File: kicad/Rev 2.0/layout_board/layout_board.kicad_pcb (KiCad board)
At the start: 2 copper layers, 309.6 x 95.2 mm, 216 parts, among them U0:0 GH39FKSW, U0:1 GH39FKSW, U0:10 GH39FKSW, U0:11 GH39FKSW, U0:12 GH39FKSW, U0:13 GH39FKSW, U0:14 GH39FKSW, U0:2 GH39FKSW, U0:3 GH39FKSW, U0:4 GH39FKSW, U0:5 GH39FKSW, U0:6 GH39FKSW, U0:7 GH39FKSW, U0:8 GH39FKSW, U0:9 GH39FKSW, U1 CD4067BPWR, U1:0 GH39FKSW, U1:1 GH39FKSW, U1:10 GH39FKSW, U1:11 GH39FKSW, U1:12 GH39FKSW, U1:13 GH39FKSW, U1:14 GH39FKSW, U1:2 GH39FKSW, U1:3 GH39FKSW, U1:4 GH39FKSW, U1:5 GH39FKSW, U1:6 GH39FKSW, U1:7 GH39FKSW, U1:8 GH39FKSW, U1:9 GH39FKSW, U2 CD4067BPWR, U2:0 GH39FKSW, U2:1 GH39FKSW, U2:10 GH39FKSW, U2:11 GH39FKSW, U2:12 GH39FKSW, U2:13 GH39FKSW, U2:2 GH39FKSW, U2:3 GH39FKSW, U2:4 GH39FKSW, U2:5 GH39FKSW, U2:6 GH39FKSW, U2:7 GH39FKSW, U2:8 GH39FKSW, U2:9 GH39FKSW, U3 CD4067BPWR, U3:1 GH39FKSW, U3:10 GH39FKSW, U3:11 GH39FKSW, U3:12 GH39FKSW, U3:13 GH39FKSW, U3:2 GH39FKSW, U3:3 GH39FKSW, U3:4 GH39FKSW, U3:5 GH39FKSW, U3:6 GH39FKSW, U3:7 GH39FKSW, U3:8 GH39FKSW, U3:9 GH39FKSW, U4 CD4067BPWR, U4:1 GH39FKSW, U4:10 GH39FKSW, U4:12 GH39FKSW, U4:13 GH39FKSW, U4:14 GH39FKSW, U4:2 GH39FKSW, U4:3 GH39FKSW, U4:5 GH39FKSW, U4:7 GH39FKSW, U4:9 GH39FKSW, U5 CD4067BPWR

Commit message: wip: rev 2.0 pcb
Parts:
- removed C1, C10, C11, C12, C13, C14, C15, C16, C17, C18, C19, C2, C20, C21, C22, C23, C24, C25, C26, C27, C28, C29, C3, C30, C31, C32, C33, C34, C35, C36, C37, C38, C39, C4, C40, C41, C42, C43, C44, C45, C46, C47, C48, C49, C5, C50, C51, C52, C53, C54, C55, C56, C57, C58, C59, C6, C60, C61, C62, C63, C64, C65, C66, C67, C7, C8, C9: 100n, Capacitor_SMD:C_0402_1005Metric_Pad0.74x0.62mm_HandSolder
- moved U3 22.0 mm to (187.2, 66.7)
- moved U5 20.6 mm to (308.0, 66.7)
- moved U4 20.6 mm to (241.3, 66.7)
- moved C69 20.5 mm to (126.6, 62.2), turned to 180 degrees
- moved U2 19.6 mm to (133.3, 66.7)
- moved U1 16.1 mm to (69.3, 66.7)
- moved C68 14.1 mm to (64.7, 61.9), turned to 180 degrees
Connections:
- U0:0 pad 2: unconnected-(U0:0-VOUT-Pad2) -> /AMUX0:10
- U0:1 pad 2: unconnected-(U0:1-VOUT-Pad2) -> /AMUX0:9
- U0:2 pad 2: unconnected-(U0:2-VOUT-Pad2) -> /AMUX0:7
- U0:3 pad 2: unconnected-(U0:3-VOUT-Pad2) -> /AMUX0:6
- U1 pad 16: /AMUX0:15 -> unconnected-(U1-15-Pad16)
- U1 pad 17: /AMUX0:14 -> unconnected-(U1-14-Pad17)
- U1:0 pad 2: unconnected-(U1:0-VOUT-Pad2) -> /AMUX0:11
- U1:1 pad 2: unconnected-(U1:1-VOUT-Pad2) -> /AMUX0:8
- U1:2 pad 2: unconnected-(U1:2-VOUT-Pad2) -> /AMUX0:5
- U2 pad 16: /AMUX1:15 -> unconnected-(U2-15-Pad16)
- U2 pad 17: /AMUX1:14 -> unconnected-(U2-14-Pad17)
- U2 pad 18: /AMUX1:13 -> unconnected-(U2-13-Pad18)
- U2:0 pad 2: unconnected-(U2:0-VOUT-Pad2) -> /AMUX0:12
- U2:1 pad 2: unconnected-(U2:1-VOUT-Pad2) -> /AMUX0:1
- U2:2 pad 2: unconnected-(U2:2-VOUT-Pad2) -> /AMUX0:4
- U3 pad 16: /AMUX2:15 -> unconnected-(U3-15-Pad16)
- U3 pad 17: /AMUX2:14 -> unconnected-(U3-14-Pad17)
- U3 pad 18: /AMUX2:13 -> unconnected-(U3-13-Pad18)
- U3:1 pad 2: unconnected-(U3:1-VOUT-Pad2) -> /AMUX0:0
- U3:2 pad 2: unconnected-(U3:2-VOUT-Pad2) -> /AMUX0:2
- U4 pad 16: /AMUX3:15 -> unconnected-(U4-15-Pad16)
- U4 pad 17: /AMUX3:14 -> unconnected-(U4-14-Pad17)
- U4 pad 18: /AMUX3:13 -> unconnected-(U4-13-Pad18)
- U4:1 pad 2: unconnected-(U4:1-VOUT-Pad2) -> /AMUX0:13
- U4:2 pad 2: unconnected-(U4:2-VOUT-Pad2) -> /AMUX0:3
- U5 pad 16: /AMUX4:15 -> unconnected-(U5-15-Pad16)
- U5 pad 17: /AMUX4:14 -> unconnected-(U5-14-Pad17)
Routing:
- net /AMUX0:3: track 0.00 -> 59.1 mm
- net /AMUX0:13: track 0.00 -> 52.4 mm
- net /AMUX0:6: track 0.00 -> 41.1 mm
- net /AMUX0:10: track 0.00 -> 40.6 mm
- net /AMUX0:2: track 0.00 -> 33.8 mm
- net /AMUX0:7: track 0.00 -> 33.5 mm
- net /AMUX0:0: track 0.00 -> 33.5 mm
- net /AMUX0:11: track 0.00 -> 32.5 mm
- net /AMUX0:12: track 0.00 -> 31.9 mm
- net /AMUX0:9: track 0.00 -> 31.7 mm
- net /SELECT2: track 219.5 -> 248.0 mm, vias 0 -> 5
- net /AMUX0:4: track 0.00 -> 27.0 mm
- net /SELECT1: track 219.1 -> 245.6 mm, vias 0 -> 5
- net /SELECT3: track 220.7 -> 245.3 mm, vias 0 -> 5
- net /AMUX0:5: track 0.00 -> 22.3 mm
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- added copper zone on F.Cu, net GND

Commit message: wip: rev 2.0 pcb
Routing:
- net +3.3VA: track 5.45 -> 246.7 mm
- net /AMUX0:5: track 22.3 -> 23.1 mm
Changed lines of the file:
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@@
 		(fp_arc
 			(start 9.03125 8.000001)
-			(mid 8.677693 7.853543)
+			(mid 8.677729 7.853537)
 			(end 8.53125 7.500001)
 			(stroke
@@
 		(fp_arc
 			(start 14.780039 -5.999999)
-			(mid 15.133602 -5.853545)
+			(mid 15.133567 -5.853539)
 			(end 15.280039 -5.499999)
 			(stroke
@@
 		(fp_arc
 			(start 15.28125 7.500001)
-			(mid 15.1348 7.853536)
+			(mid 15.134806 7.853571)
 			(end 14.78125 8.000001)
 			(stroke
@@
 		(fp_arc
 			(start 15.28125 7.500001)
-			(mid 15.1348 7.853536)
+			(mid 15.134806 7.853571)
 			(end 14.78125 8.000001)
 			(stroke
@@
 		(fp_arc
 			(start 14.780039 -5.999999)
-			(mid 15.133602 -5.853545)
+			(mid 15.133567 -5.853539)
 			(end 15.280039 -5.499999)
 			(stroke
@@
 		(fp_arc
 			(start 9.03125 8.000001)
-			(mid 8.677693 7.853543)
+			(mid 8.677729 7.853537)
 			(end 8.53125 7.500001)
 			(stroke
@@
 		(fp_arc
 			(start 15.28125 7.500001)
-			(mid 15.1348 7.853536)
+			(mid 15.134806 7.853571)
 			(end 14.78125 8.000001)
 			(stroke
@@
 		(fp_arc
 			(start 14.780039 -5.999999)
-			(mid 15.133602 -5.853545)
+			(mid 15.133567 -5.853539)
 			(end 15.280039 -5.499999)
 			(stroke
@@
 		(fp_arc
 			(start 9.03125 8.000001)
-			(mid 8.677693 7.853543)
+			(mid 8.677729 7.853537)
 			(end 8.53125 7.500001)
 			(stroke
@@
 		(fp_arc
 			(start 9.03125 8.000001)
-			(mid 8.677693 7.853543)
+			(mid 8.677729 7.853537)
 			(end 8.53125 7.500001)
 			(stroke
@@
 		(fp_arc
 			(start 14.780039 -5.999999)
-			(mid 15.133602 -5.853545)
+			(mid 15.133567 -5.853539)
 			(end 15.280039 -5.499999)
 			(stroke
@@
 		(fp_arc
 			(start 15.28125 7.500001)
-			(mid 15.1348 7.853536)
+			(mid 15.134806 7.853571)
 			(end 14.78125 8.000001)
 			(stroke
@@
 		(tags "capacitor handsolder")
 		(property "Reference" "C68"
-			(at 0 1.16 360)
+			(at 0 1.16 0)
 			(layer "B.SilkS")
 			(effects
@@
 		)
 		(property "Value" "100n"
-			(at 0 -1.16 360)
+			(at 0 -1.16 0)
 			(layer "B.Fab")
 			(effects
@@
 		)
 		(fp_text user "${REFERENCE}"
-			(at 0 0 360)
+			(at 0 0 0)
 			(layer "B.Fab")
 			(effects
@@
 		(tags "capacitor handsolder")
 		(property "Reference" "C69"
-			(at 0 1.16 360)
+			(at 0 1.16 0)
 			(layer "B.SilkS")
 			(effects
@@
 		)
 		(property "Value" "100n"
-			(at 0 -1.16 360)
+			(at 0 -1.16 0)
 			(layer "B.Fab")
 			(effects
@@
 		)
 		(fp_text user "${REFERENCE}"
-			(at 0 0 360)
+			(at 0 0 0)
 			(layer "B.Fab")
 			(effects
@@
 	)
 	(segment
+		(start 127.208669 71.402118)
+		(end 131.971169 76.164618)
+		(width 0.5)
+		(layer "B.Cu")
+		(net 2)
+	)
+	(segment
+		(start 153.402419 107.120868)
+		(end 153.402419 114.264618)
+		(width 0.5)
+		(layer "B.Cu")
+		(net 2)
+	)
+	(segment
+		(start 155.974294 38.064618)
+		(end 165.308669 47.398993)
+		(width 0.5)
+		(layer "B.Cu")
+		(net 2)
+	)
+	(segment
+		(start 151.021169 76.164618)
+		(end 141.496169 85.689618)
+		(width 0.5)
+		(layer "B.Cu")
+		(net 2)
+	)
+	(segment
+		(start 167.877984 73.971433)
+		(end 170.071169 76.164618)
+		(width 0.5)
+		(layer "B.Cu")
+		(net 2)
+	)
+	(segment
+		(start 117.683669 38.064618)
+		(end 127.208669 47.589618)
+		(width 0.5)
+		(layer "B.Cu")
+		(net 2)
+	)
+	(segment
+		(start 160.546169 85.689618)
+		(end 160.546169 95.214618)
+		(width 0.5)
+		(layer "B.Cu")
+		(net 2)
+	)
+	(segment
+		(start 146.258669 57.114618)
+		(end 146.258669 71.402118)
+		(width 0.5)
+		(layer "B.Cu")
+		(net 2)
+	)
+	(segment
 		(start 66.457912 63.099887)
 		(end 65.30768 61.949655)
@@
 	)
 	(segment
-		(start 130.569852 63.099887)
-		(end 128.072704 63.099887)
+		(start 146.258669 47.589618)
+		(end 146.258669 57.114618)
 		(width 0.5)
 		(layer "B.Cu")
@@
 	)
 	(segment
-		(start 128.072704 63.099887)
-		(end 127.182921 62.210104)
+		(start 167.877984 59.683933)
+		(end 167.877984 73.971433)
+		(width 0.5)
+		(layer "B.Cu")
+		(net 2)
+	)
+	(segment
+		(start 127.208669 57.114618)
+		(end 127.208669 71.402118)
+		(width 0.5)
+		(layer "B.Cu")
+		(net 2)
+	)
+	(segment
+		(start 122.446169 95.214618)
+		(end 120.064919 97.595868)
+		(width 0.5)
+		(layer "B.Cu")
+		(net 2)
+	)
+	(segment
+		(start 120.064919 97.595868)
+		(end 120.064919 114.264618)
+		(width 0.5)
+		(layer "B.Cu")
+		(net 2)
+	)
+	(segment
+		(start 165.308669 57.114618)
+		(end 167.877984 59.683933)
 		(width 0.5)
 		(layer "B.Cu")
@@
 	)
 	(segment
+		(start 165.308669 47.398993)
+		(end 165.308669 57.114618)
+		(width 0.5)
+		(layer "B.Cu")
+		(net 2)
+	)
+	(segment
+		(start 122.446169 85.689618)
+		(end 122.446169 95.214618)
+		(width 0.5)
+		(layer "B.Cu")
+		(net 2)
+	)
+	(segment
+		(start 136.733669 38.064618)
+		(end 146.258669 47.589618)
+		(width 0.5)
+		(layer "B.Cu")
+		(net 2)
+	)
+	(segment
+		(start 131.971169 76.164618)
+		(end 122.446169 85.689618)
+		(width 0.5)
+		(layer "B.Cu")
+		(net 2)
+	)
+	(segment
+		(start 141.496169 95.214618)
+		(end 153.402419 107.120868)
+		(width 0.5)
+		(layer "B.Cu")
+		(net 2)
+	)
+	(segment
 		(start 66.47268 63.099887)
 		(end 66.457912 63.099887)
@@
 	)
 	(segment
+		(start 127.208669 47.589618)
+		(end 127.208669 57.114618)
+		(width 0.5)
+		(layer "B.Cu")
+		(net 2)
+	)
+	(segment
+		(start 141.496169 85.689618)
+		(end 141.496169 95.214618)
+		(width 0.5)
+		(layer "B.Cu")
+		(net 2)
+	)
+	(segment
+		(start 170.071169 76.164618)
+		(end 160.546169 85.689618)
+		(width 0.5)
+		(layer "B.Cu")
+		(net 2)
+	)
+	(segment
+		(start 146.258669 71.402118)
+		(end 151.021169 76.164618)
+		(width 0.5)
+		(layer "B.Cu")
+		(net 2)
+	)
+	(segment
 		(start 65.296169 61.938144)
 		(end 65.30768 61.949655)
@@
 	)
 	(segment
-		(start 79.722588 65.049849)
-		(end 89.001268 55.771169)
+		(start 90.452118 57.185258)
+		(end 90.452118 55.771169)
 		(width 0.3)
 		(layer "B.Cu")
@@
 	)
 	(segment
-		(start 72.032752 65.049849)
-		(end 79.722588 65.049849)
+		(start 82.587527 65.049849)
+		(end 90.452118 57.185258)
 		(width 0.3)
 		(layer "B.Cu")
@@
 	)
 	(segment
-		(start 89.001268 55.771169)
-		(end 90.452118 55.771169)
+		(start 72.032752 65.049849)
+		(end 82.587527 65.049849)
 		(width 0.3)
 		(layer "B.Cu")
@@
 	)
 	(segment
-		(start 39.84654 38.503091)
-		(end 38.064618 36.721169)
+		(start 66.47268 65.049849)
+		(end 65.049849 65.049849)
 		(width 0.3)
 		(layer "B.Cu")
@@
 	)
 	(segment
-		(start 65.681684 65.049849)
-		(end 39.84654 39.214705)
+		(start 65.049849 65.049849)
+		(end 39.84654 39.84654)
 		(width 0.3)
 		(layer "B.Cu")
@@
 	)
 	(segment
-		(start 66.47268 65.049849)
-		(end 65.681684 65.049849)
+		(start 39.84654 38.503091)
+		(end 38.064618 36.721169)
 		(width 0.3)
 		(layer "B.Cu")
@@
 	)
 	(segment
-		(start 39.84654 39.214705)
+		(start 39.84654 39.84654)
 		(end 39.84654 38.503091)
 		(width 0.3)

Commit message: wip: rev 2.0 pcb
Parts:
- moved U5 24.4 mm to (300.0, 43.6), turned to 90 degrees
- moved U2 23.5 mm to (128.9, 43.6), turned to 90 degrees
- moved U1 23.1 mm to (71.5, 43.6), turned to 90 degrees
- moved U4 23.1 mm to (242.9, 43.6), turned to 90 degrees
- moved U3 23.1 mm to (185.7, 43.6), turned to 90 degrees
- moved C71 18.3 mm to (245.0, 49.5)
- moved C70 18.1 mm to (187.9, 49.5)
- moved C68 15.3 mm to (73.7, 49.6)
- moved C69 13.4 mm to (131.2, 49.6)
- moved C72 9.25 mm to (302.2, 49.6), turned to 180 degrees
- turned U0:11 to -45 degrees
- turned U0:14 to -45 degrees
- turned U0:2 to -45 degrees
- turned U0:3 to -45 degrees
- turned U0:5 to -45 degrees
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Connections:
- U0:0 pad 2: /AMUX0:10 -> /AMUX0:1
- U0:1 pad 2: /AMUX0:9 -> /AMUX0:0
- U0:10 pad 2: unconnected-(U0:10-VOUT-Pad2) -> /AMUX3:0
- U0:11 pad 2: unconnected-(U0:11-VOUT-Pad2) -> /AMUX3:12
- U0:12 pad 2: unconnected-(U0:12-VOUT-Pad2) -> /AMUX4:1
- U0:13 pad 2: unconnected-(U0:13-VOUT-Pad2) -> /AMUX4:0
- U0:14 pad 2: unconnected-(U0:14-VOUT-Pad2) -> /AMUX4:13
- U0:2 pad 2: /AMUX0:7 -> /AMUX0:13
- U0:3 pad 2: /AMUX0:6 -> /AMUX0:12
- U0:4 pad 2: unconnected-(U0:4-VOUT-Pad2) -> /AMUX1:0
- U0:5 pad 2: unconnected-(U0:5-VOUT-Pad2) -> /AMUX1:12
- U0:6 pad 2: unconnected-(U0:6-VOUT-Pad2) -> /AMUX2:1
- U0:7 pad 2: unconnected-(U0:7-VOUT-Pad2) -> /AMUX2:0
- U0:8 pad 2: unconnected-(U0:8-VOUT-Pad2) -> /AMUX2:12
- U0:9 pad 2: unconnected-(U0:9-VOUT-Pad2) -> /AMUX3:1
- U1:0 pad 2: /AMUX0:11 -> /AMUX0:2
- U1:1 pad 2: /AMUX0:8 -> /AMUX0:7
- U1:10 pad 2: unconnected-(U1:10-VOUT-Pad2) -> /AMUX3:7
- U1:11 pad 2: unconnected-(U1:11-VOUT-Pad2) -> /AMUX3:11
- U1:12 pad 2: unconnected-(U1:12-VOUT-Pad2) -> /AMUX4:4
- U1:13 pad 2: unconnected-(U1:13-VOUT-Pad2) -> /AMUX4:8
- U1:14 pad 2: unconnected-(U1:14-VOUT-Pad2) -> /AMUX4:12
- U1:2 pad 2: /AMUX0:5 -> /AMUX0:10
- U1:3 pad 2: unconnected-(U1:3-VOUT-Pad2) -> /AMUX1:2
- U1:4 pad 2: unconnected-(U1:4-VOUT-Pad2) -> /AMUX1:7
- U1:5 pad 2: unconnected-(U1:5-VOUT-Pad2) -> /AMUX1:10
- U1:6 pad 2: unconnected-(U1:6-VOUT-Pad2) -> /AMUX2:3
- U1:7 pad 2: unconnected-(U1:7-VOUT-Pad2) -> /AMUX2:7
- U1:8 pad 2: unconnected-(U1:8-VOUT-Pad2) -> /AMUX2:10
- U1:9 pad 2: unconnected-(U1:9-VOUT-Pad2) -> /AMUX3:3
- U2:0 pad 2: /AMUX0:12 -> /AMUX0:3
- U2:1 pad 2: /AMUX0:1 -> /AMUX0:6
- U2:10 pad 2: unconnected-(U2:10-VOUT-Pad2) -> /AMUX3:8
- U2:11 pad 2: unconnected-(U2:11-VOUT-Pad2) -> /AMUX4:2
- U2:12 pad 2: unconnected-(U2:12-VOUT-Pad2) -> /AMUX4:5
- U2:13 pad 2: unconnected-(U2:13-VOUT-Pad2) -> /AMUX4:7
- U2:2 pad 2: /AMUX0:4 -> /AMUX0:11
- U2:3 pad 2: unconnected-(U2:3-VOUT-Pad2) -> /AMUX1:3
- U2:4 pad 2: unconnected-(U2:4-VOUT-Pad2) -> /AMUX1:6
- U2:5 pad 2: unconnected-(U2:5-VOUT-Pad2) -> /AMUX1:11
- U2:6 pad 2: unconnected-(U2:6-VOUT-Pad2) -> /AMUX2:4
- U2:7 pad 2: unconnected-(U2:7-VOUT-Pad2) -> /AMUX2:6
- U2:8 pad 2: unconnected-(U2:8-VOUT-Pad2) -> /AMUX2:11
- U2:9 pad 2: unconnected-(U2:9-VOUT-Pad2) -> /AMUX3:4
- U3:1 pad 2: /AMUX0:0 -> /AMUX0:5
- U3:10 pad 2: unconnected-(U3:10-VOUT-Pad2) -> /AMUX3:6
- U3:11 pad 2: unconnected-(U3:11-VOUT-Pad2) -> /AMUX3:9
- U3:12 pad 2: unconnected-(U3:12-VOUT-Pad2) -> /AMUX4:3
- U3:13 pad 2: unconnected-(U3:13-VOUT-Pad2) -> /AMUX4:10
- U3:2 pad 2: /AMUX0:2 -> /AMUX0:8
- U3:3 pad 2: unconnected-(U3:3-VOUT-Pad2) -> /AMUX1:1
- U3:4 pad 2: unconnected-(U3:4-VOUT-Pad2) -> /AMUX1:5
- U3:5 pad 2: unconnected-(U3:5-VOUT-Pad2) -> /AMUX1:8
- U3:6 pad 2: unconnected-(U3:6-VOUT-Pad2) -> /AMUX2:2
- U3:7 pad 2: unconnected-(U3:7-VOUT-Pad2) -> /AMUX2:5
- U3:8 pad 2: unconnected-(U3:8-VOUT-Pad2) -> /AMUX2:8
- U3:9 pad 2: unconnected-(U3:9-VOUT-Pad2) -> /AMUX3:2
- U4:1 pad 2: /AMUX0:13 -> /AMUX0:4
- U4:10 pad 2: unconnected-(U4:10-VOUT-Pad2) -> /AMUX3:10
- U4:12 pad 2: unconnected-(U4:12-VOUT-Pad2) -> /AMUX4:6
- U4:13 pad 2: unconnected-(U4:13-VOUT-Pad2) -> /AMUX4:9
- U4:14 pad 2: unconnected-(U4:14-VOUT-Pad2) -> /AMUX4:11
- U4:2 pad 2: /AMUX0:3 -> /AMUX0:9
- U4:3 pad 2: unconnected-(U4:3-VOUT-Pad2) -> /AMUX1:4
- U4:5 pad 2: unconnected-(U4:5-VOUT-Pad2) -> /AMUX1:9
- U4:7 pad 2: unconnected-(U4:7-VOUT-Pad2) -> /AMUX2:9
- U4:9 pad 2: unconnected-(U4:9-VOUT-Pad2) -> /AMUX3:5
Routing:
- net +3.3VA: track 246.7 -> 1992.0 mm, vias 0 -> 51
- net /ADC4: track 0.00 -> 265.9 mm, vias 0 -> 1
- net /ADC3: track 0.00 -> 208.2 mm, vias 0 -> 1
- net /ADC2: track 0.00 -> 150.4 mm, vias 0 -> 1
- net /ADC1: track 0.00 -> 93.1 mm, vias 0 -> 1
- net /AMUX4:11: track 0.00 -> 89.1 mm
- net /AMUX1:9: track 0.00 -> 78.5 mm
- net /AMUX3:5: track 0.00 -> 77.5 mm
- net /AMUX1:4: track 0.00 -> 76.3 mm
- net /AMUX3:10: track 0.00 -> 76.0 mm
- net /AMUX2:9: track 0.00 -> 74.8 mm
- net /AMUX4:6: track 0.00 -> 72.3 mm
- net /AMUX1:1: track 0.00 -> 71.6 mm
- net /AMUX4:9: track 0.00 -> 70.5 mm
- net /AMUX3:2: track 0.00 -> 70.3 mm
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
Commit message: wip: working on flex cable
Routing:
- net GND: vias 3249 -> 3243

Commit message: wip: flex connector
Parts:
- added J1: Conn_01x11_Socket, Custom:Flex Cable connector, F.Cu at (54.8, 32.9)
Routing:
- net +3.3VA: track 1992.0 -> 2000.8 mm, vias 51 -> 50
- net /ADC4: track 265.9 -> 261.0 mm
- net /ADC3: track 208.2 -> 203.4 mm
- net /ADC2: track 150.4 -> 145.5 mm
- net /ADC1: track 93.1 -> 88.2 mm
- net /ADC0: track 35.1 -> 30.2 mm
- net /SELECT0: track 305.8 -> 301.2 mm
- net /SELECT1: track 303.7 -> 299.2 mm
- net /SELECT2: track 310.5 -> 306.1 mm
- net /SELECT3: track 307.0 -> 302.7 mm
- net GND: vias 3243 -> 3252
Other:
- outline, holes or cut-outs redrawn

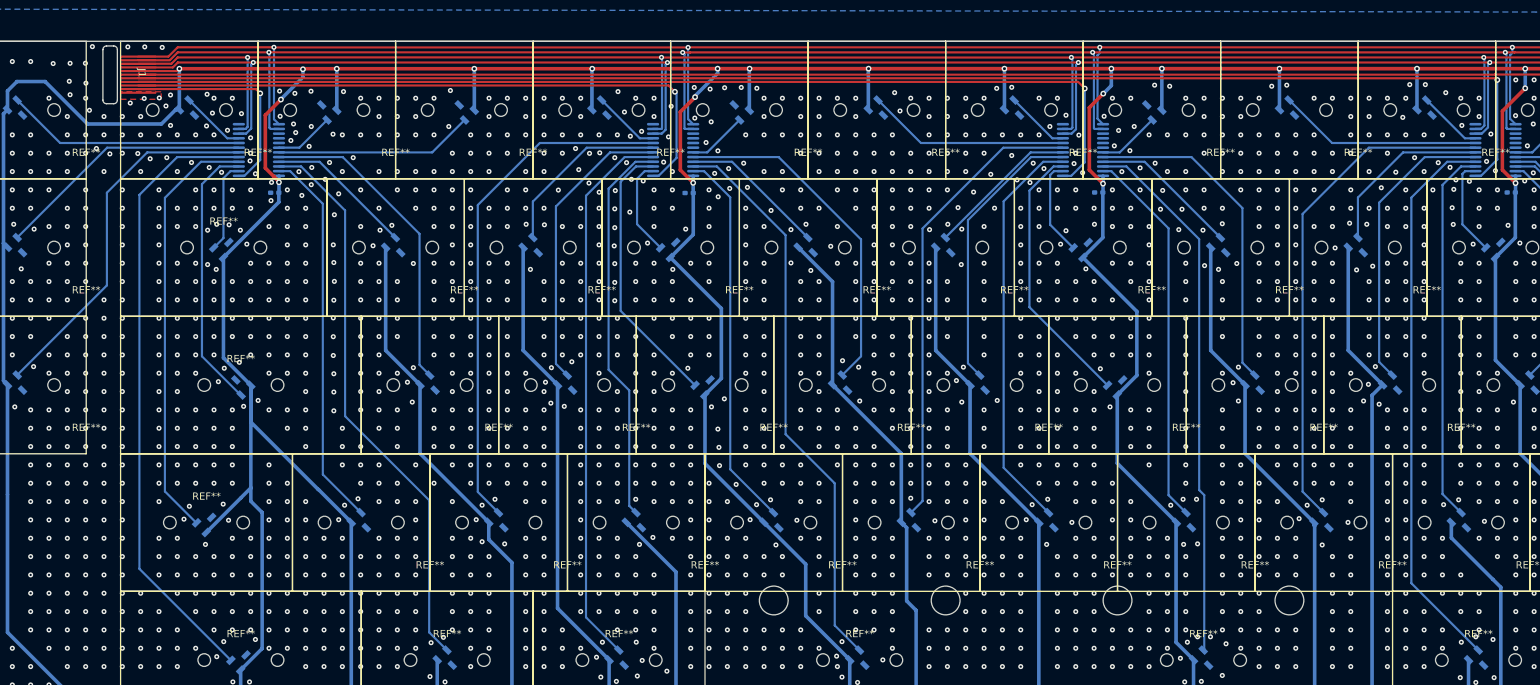
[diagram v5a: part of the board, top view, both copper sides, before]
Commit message: wip: add connector on layout board
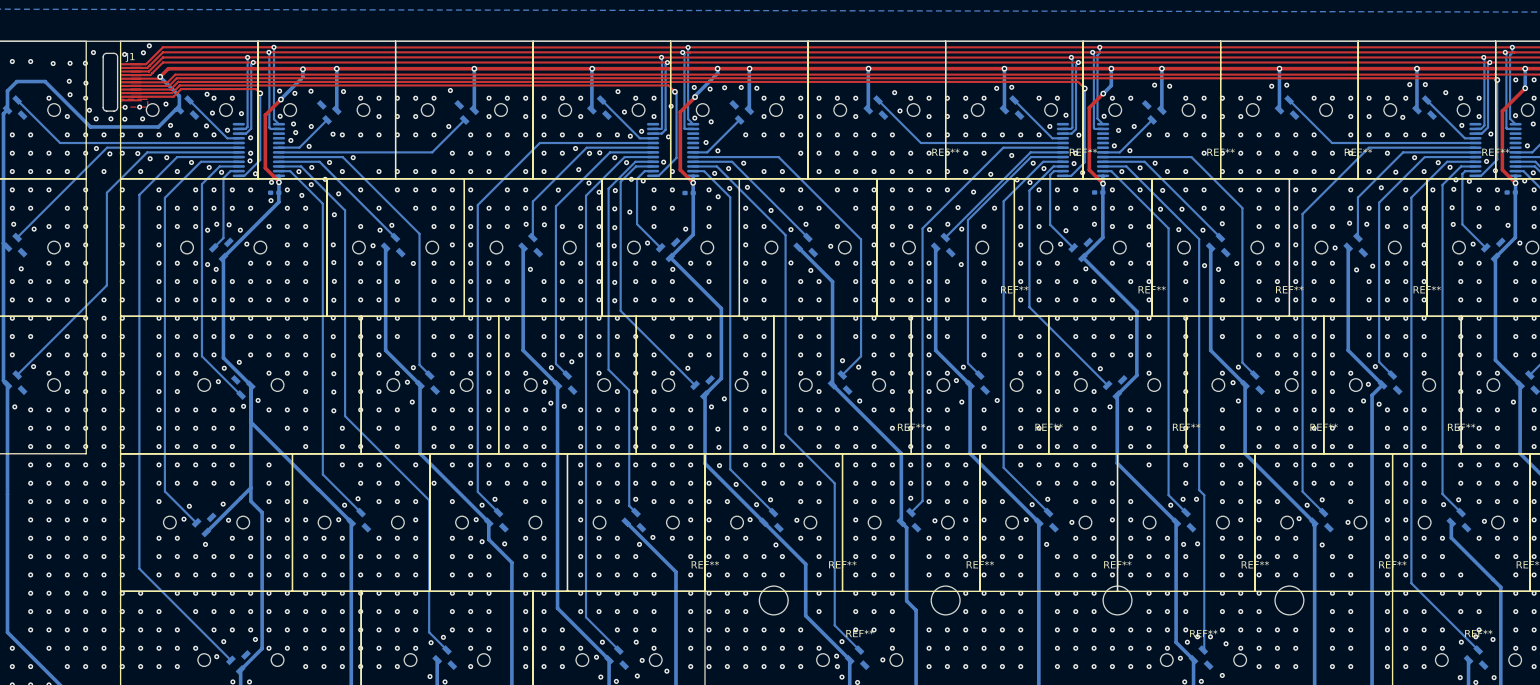
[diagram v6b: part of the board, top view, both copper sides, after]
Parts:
- moved J1 1.46 mm to (53.8, 34.0)
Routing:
- net +3.3VA: track 2000.8 -> 2002.6 mm
- net /SELECT0: track 301.2 -> 302.7 mm
- net /SELECT1: track 299.2 -> 300.6 mm
- net /SELECT2: track 306.1 -> 307.6 mm
- net /ADC3: track 203.4 -> 204.8 mm
- net /ADC2: track 145.5 -> 147.0 mm
- net /SELECT3: track 302.7 -> 304.1 mm
- net /ADC4: track 261.0 -> 262.5 mm
- net /ADC1: track 88.2 -> 89.7 mm
- net /ADC0: track 30.2 -> 31.7 mm
- net GND: vias 3252 -> 3251
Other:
- outline, holes or cut-outs redrawn
